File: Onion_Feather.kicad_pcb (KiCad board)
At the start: 4 copper layers, 59.7 x 53.3 mm, 61 parts, among them IC1 MAX11646EUA+T, J1 HR911105A, J2 CON_HEADER_PRG_AVR_ICSP-PTH, J3 Conn_01x02, J4 USB_A, J5 M04PTH, U1 ONION-OMEGA2, U2 AP1117-33, U3 CP2102N-A01-GQFN24, U4 BQ25895RTW, U5 STF202-22T1G

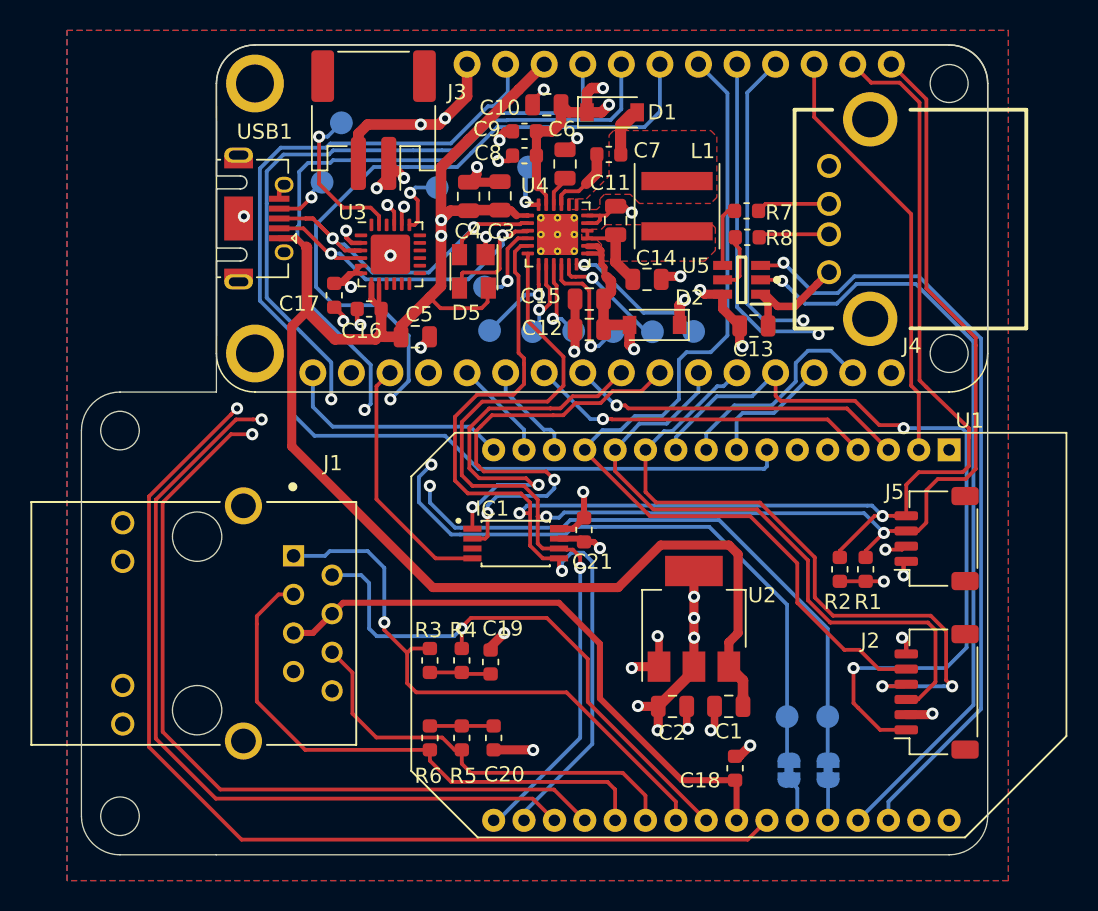
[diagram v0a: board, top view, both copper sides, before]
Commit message: PCB update, edge vias
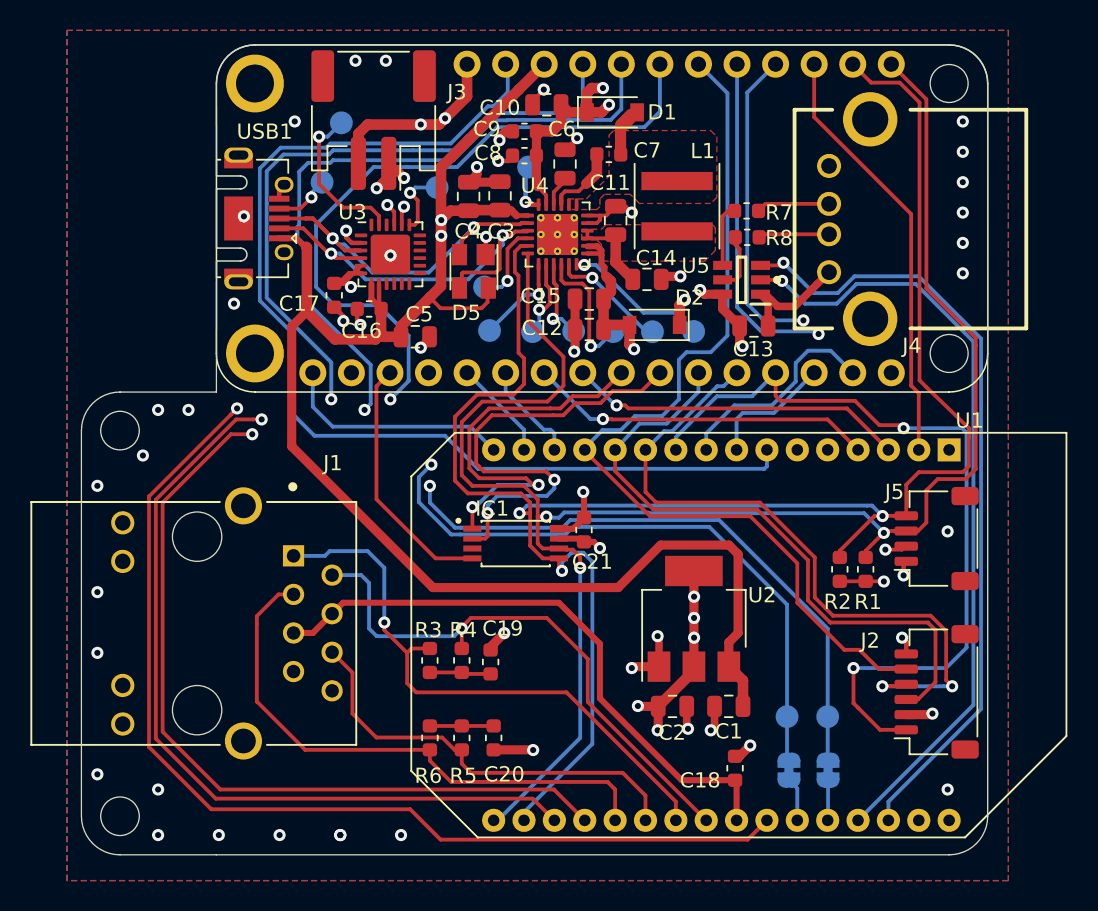
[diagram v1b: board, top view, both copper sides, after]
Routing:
- net GND: vias 29 -> 55
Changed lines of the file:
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@@
     (thickness 1.6)
     (drawings 17)
-    (tracks 1000)
+    (tracks 1028)
     (zones 0)
     (modules 61)
@@
     (46 B.CrtYd user)
     (47 F.CrtYd user)
-    (48 B.Fab user)
+    (48 B.Fab user hide)
     (49 F.Fab user)
   )
@@
       (effects (font (size 1 1) (thickness 0.15)))
     )
-    (fp_text value MAX11646EUA+T (at -0.226147 2.1966) (layer B.Adhes)
+    (fp_text value MAX11646EUA+T (at -0.226147 2.1966) (layer B.Adhes) hide
       (effects (font (size 0.480306 0.480306) (thickness 0.05)))
     )
@@
   (segment (start 145.99 101.908) (end 144.292 101.908) (width 0.6) (layer F.Cu) (net 1))
   (segment (start 144.292 101.908) (end 144.2 102) (width 0.6) (layer F.Cu) (net 1))
+  (via (at 166 70) (size 0.8) (drill 0.4) (layers F.Cu B.Cu) (net 1))
+  (via (at 166 72) (size 0.8) (drill 0.4) (layers F.Cu B.Cu) (net 1))
+  (via (at 166 74) (size 0.8) (drill 0.4) (layers F.Cu B.Cu) (net 1))
+  (via (at 166 76) (size 0.8) (drill 0.4) (layers F.Cu B.Cu) (net 1))
+  (via (at 166 68) (size 0.8) (drill 0.4) (layers F.Cu B.Cu) (net 1))
+  (via (at 165 93) (size 0.8) (drill 0.4) (layers F.Cu B.Cu) (net 1))
+  (via (at 165 110) (size 0.8) (drill 0.4) (layers F.Cu B.Cu) (net 1))
+  (via (at 129 113) (size 0.8) (drill 0.4) (layers F.Cu B.Cu) (net 1))
+  (via (at 125 113) (size 0.8) (drill 0.4) (layers F.Cu B.Cu) (net 1))
+  (via (at 125 113) (size 0.8) (drill 0.4) (layers F.Cu B.Cu) (net 1))
+  (via (at 121 113) (size 0.8) (drill 0.4) (layers F.Cu B.Cu) (net 1))
+  (via (at 117 113) (size 0.8) (drill 0.4) (layers F.Cu B.Cu) (net 1))
+  (via (at 113 113) (size 0.8) (drill 0.4) (layers F.Cu B.Cu) (net 1))
+  (via (at 113 110) (size 0.8) (drill 0.4) (layers F.Cu B.Cu) (net 1))
+  (via (at 109 109) (size 0.8) (drill 0.4) (layers F.Cu B.Cu) (net 1))
+  (via (at 109 97) (size 0.8) (drill 0.4) (layers F.Cu B.Cu) (net 1))
+  (via (at 109 101) (size 0.8) (drill 0.4) (layers F.Cu B.Cu) (net 1))
+  (via (at 109 90) (size 0.8) (drill 0.4) (layers F.Cu B.Cu) (net 1))
+  (via (at 112 88) (size 0.8) (drill 0.4) (layers F.Cu B.Cu) (net 1))
+  (via (at 113 85) (size 0.8) (drill 0.4) (layers F.Cu B.Cu) (net 1))
+  (via (at 115 85) (size 0.8) (drill 0.4) (layers F.Cu B.Cu) (net 1))
+  (via (at 118 78) (size 0.8) (drill 0.4) (layers F.Cu B.Cu) (net 1))
+  (via (at 122 66) (size 0.8) (drill 0.4) (layers F.Cu B.Cu) (net 1))
+  (via (at 126 62) (size 0.8) (drill 0.4) (layers F.Cu B.Cu) (net 1))
+  (via (at 128 62) (size 0.8) (drill 0.4) (layers F.Cu B.Cu) (net 1))
+  (via (at 166 66) (size 0.8) (drill 0.4) (layers F.Cu B.Cu) (net 1))
   (segment (start 127.05 77.7125) (end 127.6875 78.35) (width 0.4) (layer F.Cu) (net 2))
   (segment (start 127.05 76.6875) (end 127.05 77.7125) (width 0.4) (layer F.Cu) (net 2))
@@
   (segment (start 118.2 84.9) (end 123.8 84.9) (width 0.25) (layer In2.Cu) (net 36))
   (segment (start 124.404001 81.867591) (end 124.404001 84.295999) (width 0.25) (layer B.Cu) (net 36))
+  (segment (start 117.800001 85.299999) (end 118.2 84.9) (width 0.25) (layer F.Cu) (net 36))
   (segment (start 112.39998 107.19998) (end 112.39998 90.70002) (width 0.25) (layer F.Cu) (net 36))
-  (segment (start 118.5 113.3) (end 112.39998 107.19998) (width 0.25) (layer F.Cu) (net 36))
   (segment (start 153.1 112.03) (end 151.83 113.3) (width 0.25) (layer F.Cu) (net 36))
-  (segment (start 117.800001 85.299999) (end 118.2 84.9) (width 0.25) (layer F.Cu) (net 36))
+  (segment (start 151.83 113.3) (end 131.6 113.3) (width 0.25) (layer F.Cu) (net 36))
   (segment (start 112.39998 90.70002) (end 117.800001 85.299999) (width 0.25) (layer F.Cu) (net 36))
-  (segment (start 151.83 113.3) (end 118.5 113.3) (width 0.25) (layer F.Cu) (net 36))
+  (segment (start 131.6 113.3) (end 129.6 111.3) (width 0.25) (layer F.Cu) (net 36))
+  (segment (start 116.5 111.3) (end 112.39998 107.19998) (width 0.25) (layer F.Cu) (net 36))
+  (segment (start 129.6 111.3) (end 116.5 111.3) (width 0.25) (layer F.Cu) (net 36))
   (via (at 126.6 85) (size 0.8) (drill 0.4) (layers F.Cu B.Cu) (net 37))
   (segment (start 126.999999 84.600001) (end 126.6 85) (width 0.25) (layer B.Cu) (net 37))

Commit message: Add 3d models , silkscreen and renders
Signed-off-by: Tisham Dhar <whatnickd@gmail.com>
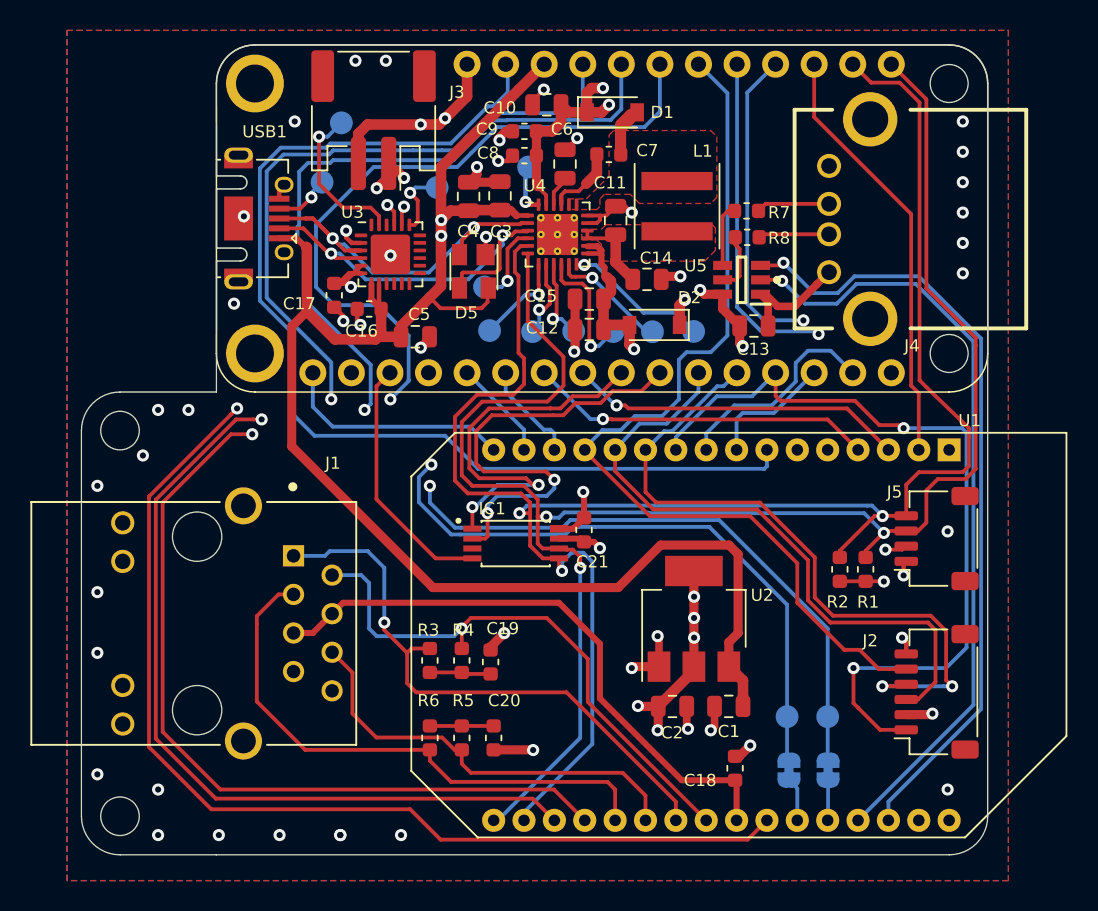
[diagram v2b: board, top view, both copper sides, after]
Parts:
- added REF**: OSHW-Logo2_7.3x6mm_SilkScreen, Symbol:OSHW-Logo2_7.3x6mm_SilkScreen, B.Cu at (135.3, 103.5)
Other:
- board text added: "Onion-Omega to Feather Adapter v0.0.1 20/04/2020 by Tisham (whatnick) Dhar OSHW TAPR"

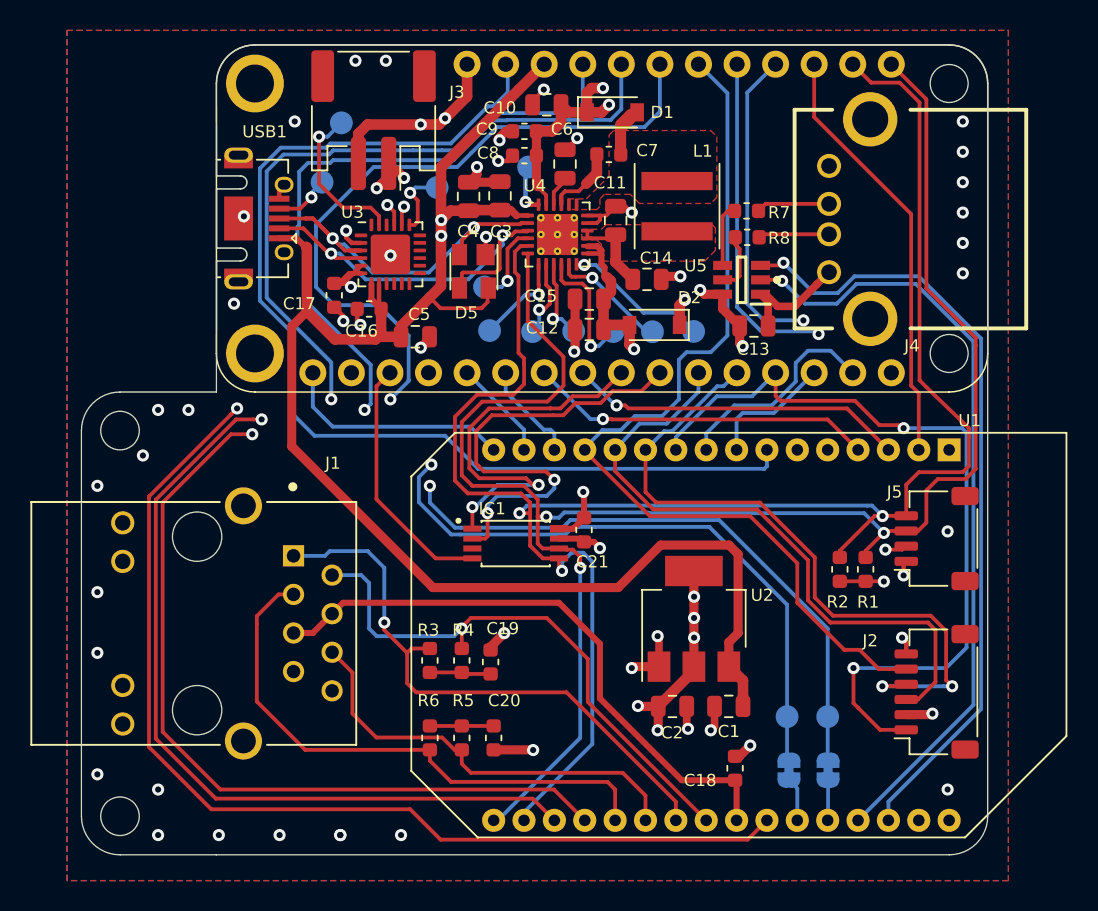
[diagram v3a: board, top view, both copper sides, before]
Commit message: #3 Correct battery connector and align PCB/Schema
Signed-off-by: Tisham Dhar <whatnickd@gmail.com>
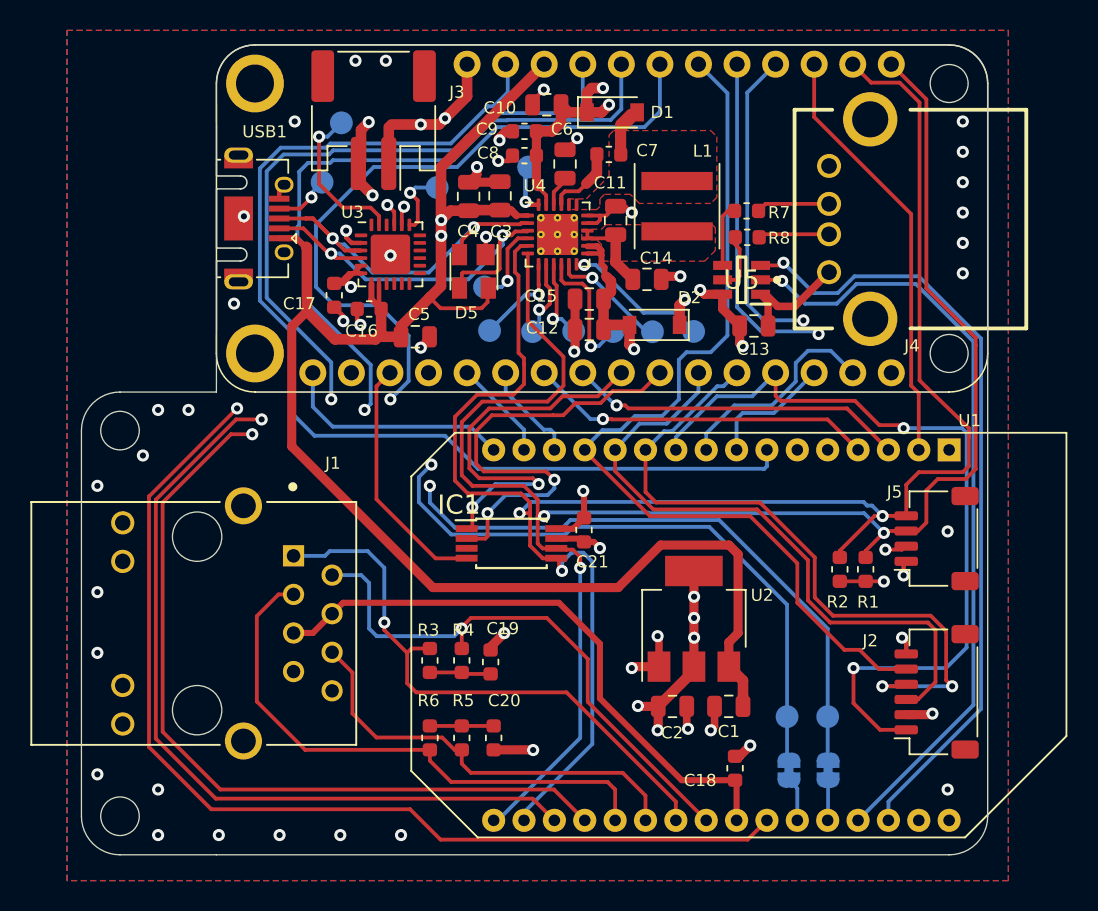
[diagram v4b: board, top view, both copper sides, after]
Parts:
- removed REF**: OSHW-Logo2_7.3x6mm_SilkScreen, Symbol:OSHW-Logo2_7.3x6mm_SilkScreen
- IC1: footprint SOP65P490X110-8N -> Package_SO:TSSOP-8_4.4x3mm_P0.65mm
- U5: footprint SOT95P275X110-6N -> footprints:SOT95P275X110-6N
- moved IC1 0.33 mm to (136.3, 93.8)
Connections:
- IC1 pad 3: (no net) -> Net-(IC1-Pad3)
- J1 pad 10: (no net) -> Net-(J1-Pad10)
- J1 pad 11: (no net) -> Net-(J1-Pad11)
- J1 pad 12: (no net) -> Net-(J1-Pad12)
- J1 pad 9: (no net) -> Net-(J1-Pad9)
- J3 pad 1: GND -> VBAT
- J3 pad 2: VBAT -> GND
- MS1 pad 16: (no net) -> Net-(MS1-Pad16)
- U3 pad 1: (no net) -> Net-(U3-Pad1)
- U3 pad 10: (no net) -> Net-(U3-Pad10)
- U3 pad 11: (no net) -> Net-(U3-Pad11)
- U3 pad 12: (no net) -> Net-(U3-Pad12)
- U3 pad 13: (no net) -> Net-(U3-Pad13)
- U3 pad 14: (no net) -> Net-(U3-Pad14)
- U3 pad 15: (no net) -> Net-(U3-Pad15)
- U3 pad 16: (no net) -> Net-(U3-Pad16)
- U3 pad 17: (no net) -> Net-(U3-Pad17)
- U3 pad 18: (no net) -> Net-(U3-Pad18)
- U3 pad 22: (no net) -> Net-(U3-Pad22)
- U3 pad 24: (no net) -> Net-(U3-Pad24)
- U3 pad 9: (no net) -> Net-(U3-Pad9)
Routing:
- net GND: track 51.7 -> 53.8 mm, vias 55 -> 54
- net VBAT: track 53.1 -> 52.2 mm

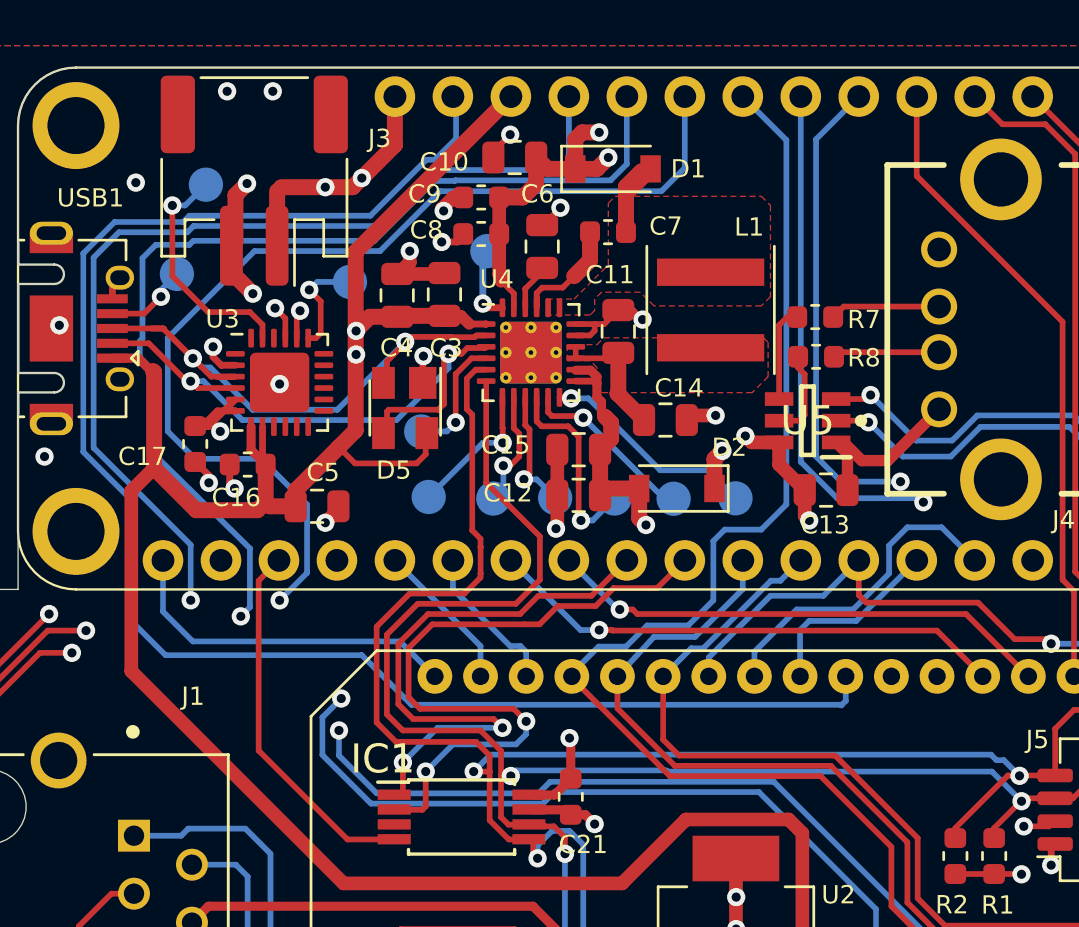
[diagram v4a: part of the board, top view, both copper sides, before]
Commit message: #6 Fix CE and TS pins
Signed-off-by: Tisham Dhar <whatnickd@gmail.com>
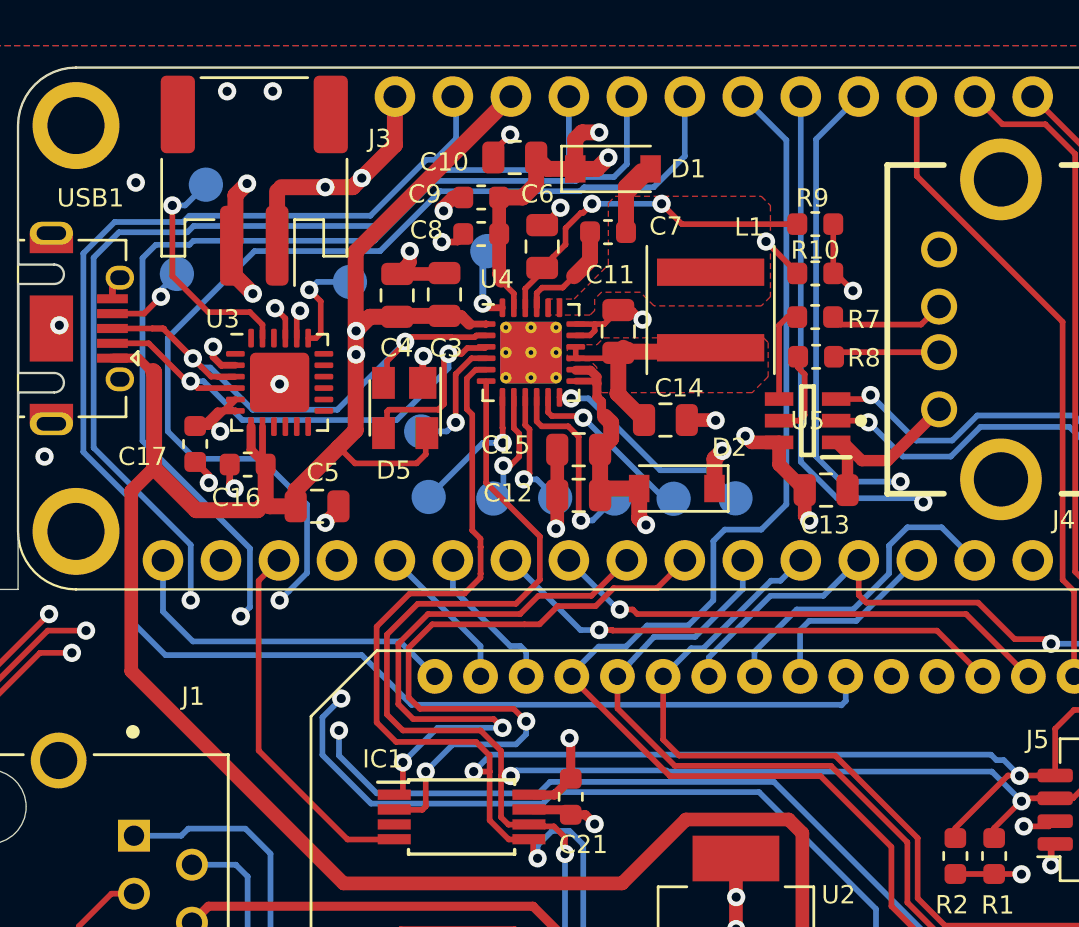
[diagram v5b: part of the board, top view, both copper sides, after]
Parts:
- added R10: 10K, Resistor_SMD:R_0603_1608Metric, F.Cu at (151.8, 70.0)
- added R9: 10K, Resistor_SMD:R_0603_1608Metric, F.Cu at (151.8, 67.8)
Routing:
- net /Power Subsystems/TS: track 7.72 -> 25.2 mm, vias 1 -> 2
- net Net-(C6-Pad1): track 1.74 -> 14.9 mm, vias 0 -> 2
- net /Power Subsystems/SYS: track 5.90 -> 10.2 mm
- net GND: track 53.8 -> 55.7 mm, vias 54 -> 55
